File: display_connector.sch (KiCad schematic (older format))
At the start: 20 parts

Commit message: Added power supply and thermosthat control circuitry.
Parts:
- removed Q?: Q_NMOS_DGS, symbol Device:Q_NMOS_DGS
- added Q?: BSS806NL6327, symbol Device:Q_NMOS_GSD
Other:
- note removed: "30V-1A NMOS sufficient, E-Lab has plenty on stock"
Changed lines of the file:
@@
 $Descr A4 11693 8268
 encoding utf-8
-Sheet 3 3
+Sheet 3 5
 Title ""
 Date ""
@@
 	1650 2500 1650 2450
 $Comp
-L Device:Q_NMOS_DGS Q?
-U 1 1 5E66CACB
-P 2250 3250
-F 0 "Q?" H 2454 3296 50  0000 L CNN
-F 1 "Q_NMOS_DGS" H 2454 3205 50  0000 L CNN
-F 2 "" H 2450 3350 50  0001 C CNN
-F 3 "~" H 2250 3250 50  0001 C CNN
-	1    2250 3250
-	1    0    0    -1
-$EndComp
-$Comp
 L Device:R R?
 U 1 1 5E66D42D
@@
 Text Notes 7050 6900 0    100  ~ 0
 Connector and support circuit for E-Paper
-Text Notes 3050 3350 0    50   ~ 0
-30V-1A NMOS sufficient, E-Lab has plenty on stock
+$Comp
+L Device:Q_NMOS_GSD Q?
+U 1 1 5E8AA986
+P 2250 3250
+F 0 "Q?" H 2455 3296 50  0000 L CNN
+F 1 "BSS806NL6327" H 2455 3205 50  0000 L CNN
+F 2 "" H 2450 3350 50  0001 C CNN
+F 3 "~" H 2250 3250 50  0001 C CNN
+	1    2250 3250
+	1    0    0    -1
+$EndComp
 $EndSCHEMATC

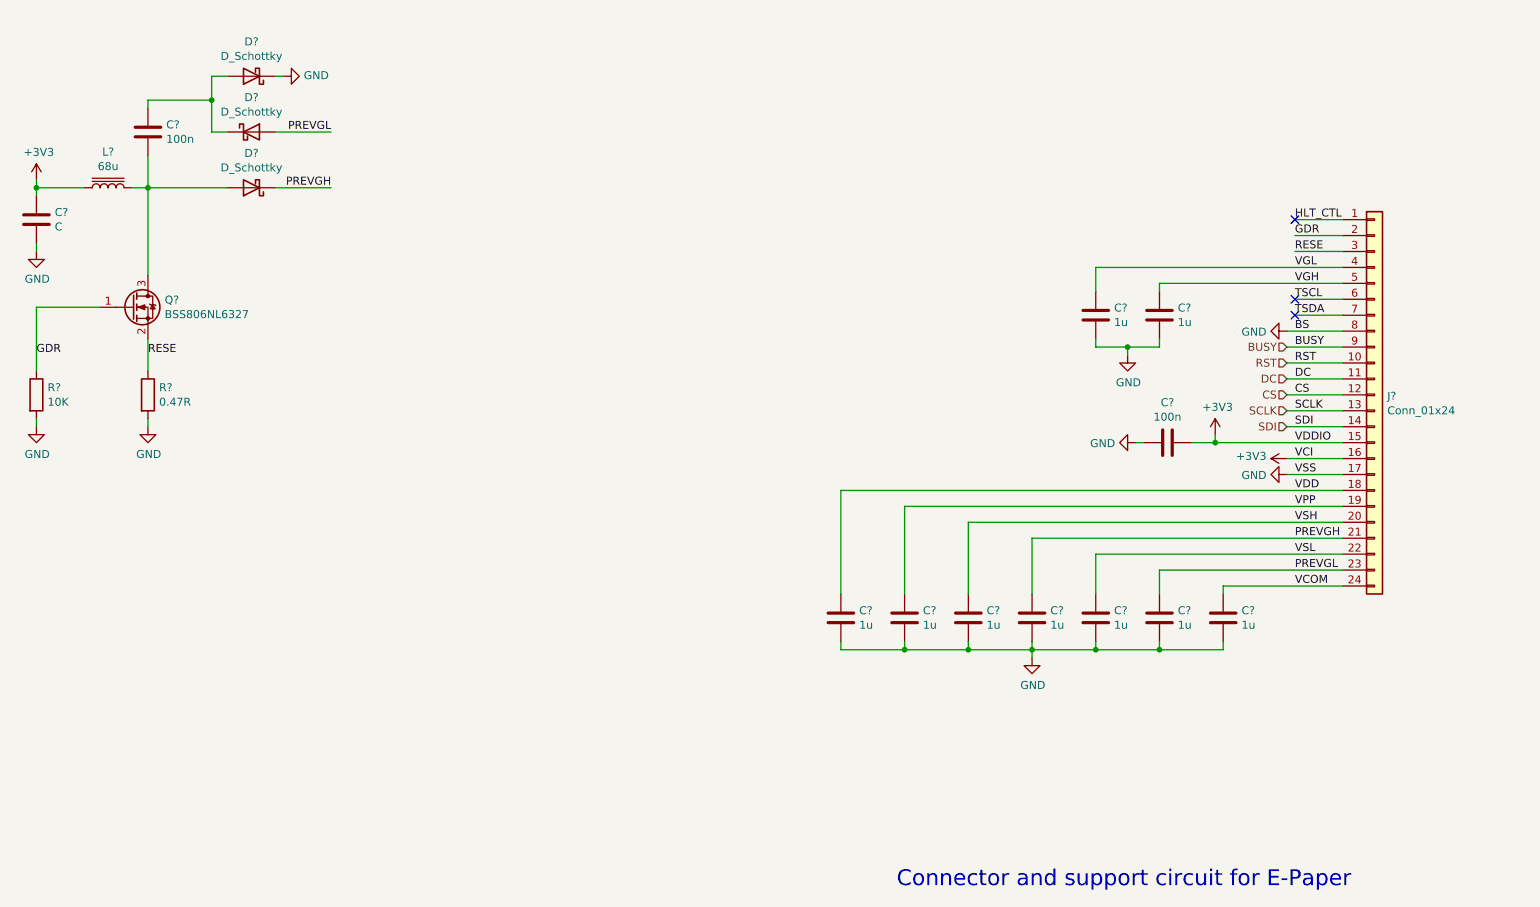
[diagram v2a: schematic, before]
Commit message: Added Temperature sensor.
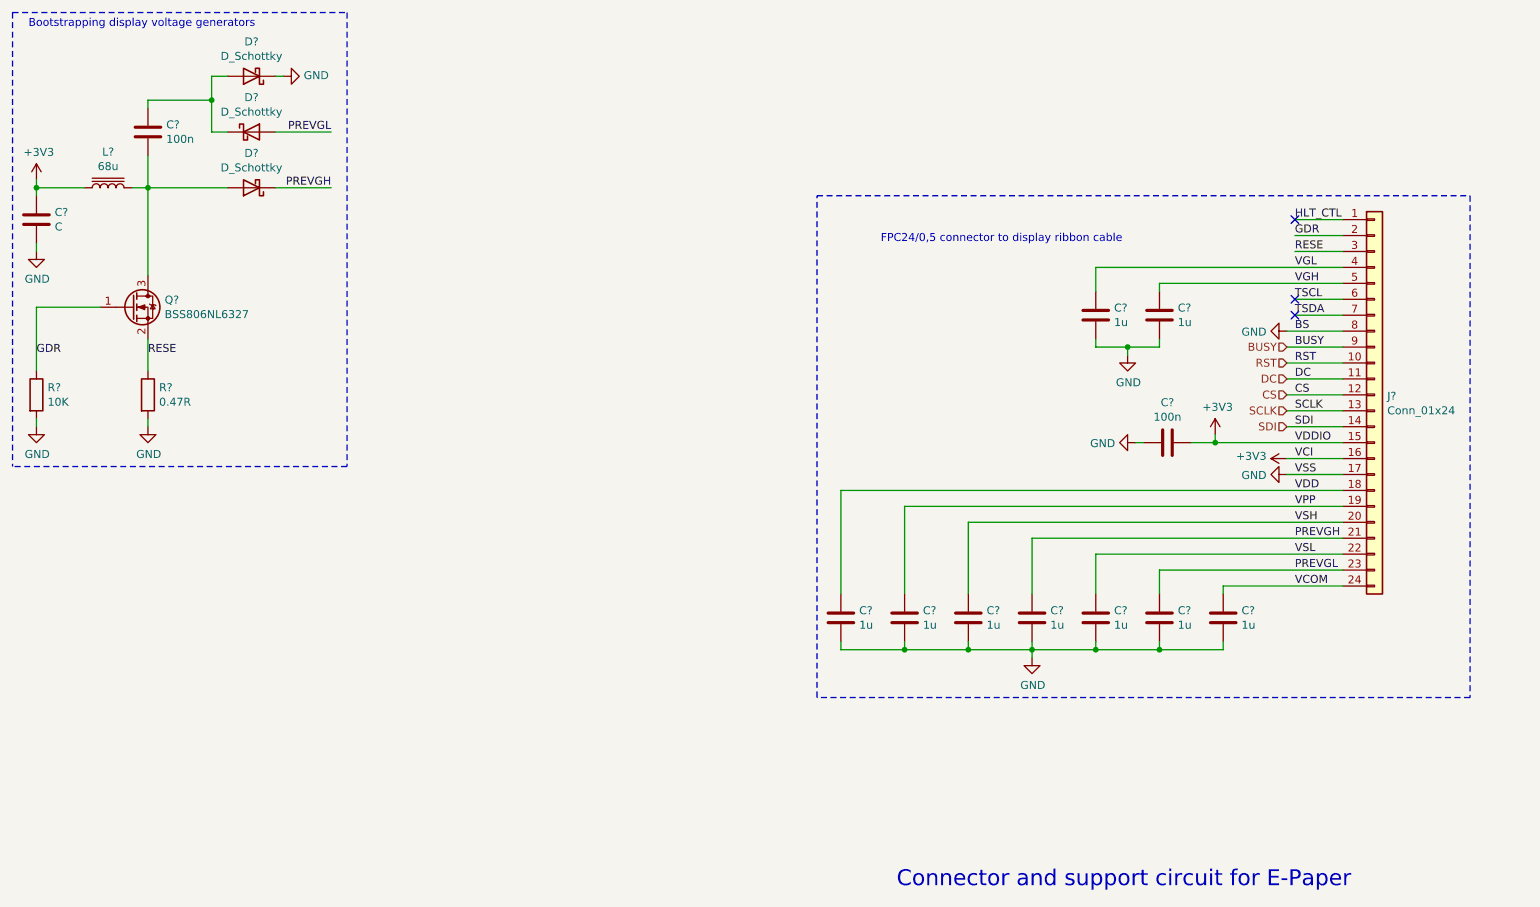
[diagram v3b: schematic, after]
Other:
- note added: "Bootstrapping display voltage generators"
- note added: "FPC24/0,5 connector to display ribbon cable"
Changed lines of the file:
@@
 $Descr A4 11693 8268
 encoding utf-8
-Sheet 3 4
+Sheet 2 4
 Title ""
 Date ""
@@
 	1    0    0    -1
 $EndComp
+Text Notes 6950 2850 0    50   ~ 0
+FPC24/0,5 connector to display ribbon cable
+Wire Notes Line
+	10650 2550 10650 5700
+Wire Notes Line
+	10650 5700 6550 5700
+Wire Notes Line
+	6550 5700 6550 2550
+Wire Notes Line
+	6550 2550 10650 2550
+Text Notes 1600 1500 0    50   ~ 0
+Bootstrapping display voltage generators
+Wire Notes Line
+	1500 1400 3600 1400
+Wire Notes Line
+	3600 1400 3600 4250
+Wire Notes Line
+	3600 4250 1500 4250
+Wire Notes Line
+	1500 1400 1500 4250
 $EndSCHEMATC
